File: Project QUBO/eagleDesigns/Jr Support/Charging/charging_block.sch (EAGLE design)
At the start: 123 parts

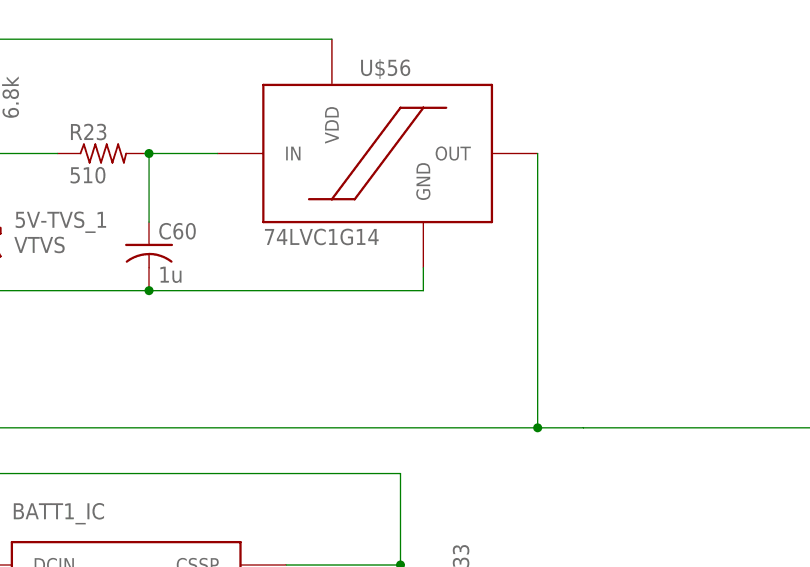
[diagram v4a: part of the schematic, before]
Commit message: 
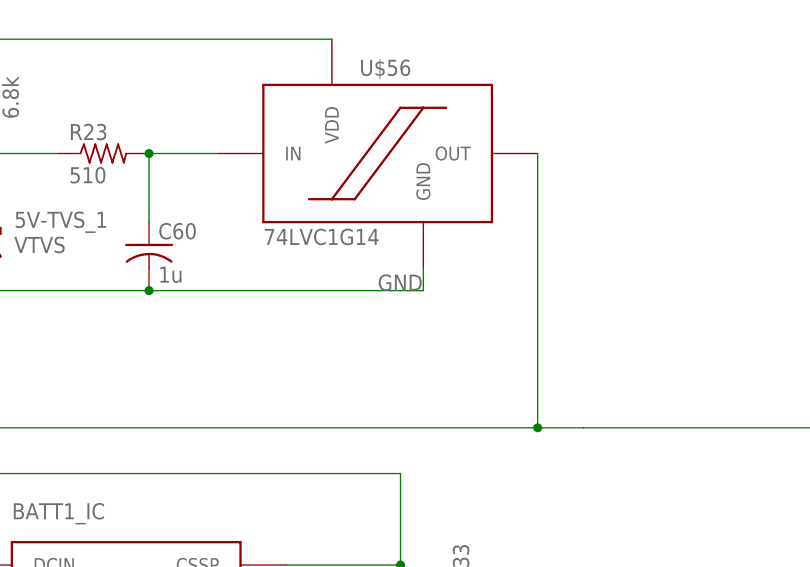
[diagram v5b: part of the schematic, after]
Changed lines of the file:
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@@
 <grid distance="0.1" unitdist="inch" unit="inch" style="lines" multiple="1" display="no" altdistance="0.01" altunitdist="inch" altunit="inch"/>
 <layers>
-<layer number="1" name="Top" color="4" fill="1" visible="yes" active="no"/>
-<layer number="2" name="Route2" color="1" fill="3" visible="yes" active="no"/>
-<layer number="3" name="Route3" color="4" fill="3" visible="yes" active="no"/>
-<layer number="4" name="Route4" color="1" fill="4" visible="yes" active="no"/>
-<layer number="5" name="Route5" color="4" fill="4" visible="yes" active="no"/>
-<layer number="6" name="Route6" color="1" fill="8" visible="yes" active="no"/>
-<layer number="7" name="Route7" color="4" fill="8" visible="yes" active="no"/>
-<layer number="8" name="Route8" color="1" fill="2" visible="yes" active="no"/>
-<layer number="9" name="Route9" color="4" fill="2" visible="yes" active="no"/>
-<layer number="10" name="Route10" color="1" fill="7" visible="yes" active="no"/>
-<layer number="11" name="Route11" color="4" fill="7" visible="yes" active="no"/>
-<layer number="12" name="Route12" color="1" fill="5" visible="yes" active="no"/>
-<layer number="13" name="Route13" color="4" fill="5" visible="yes" active="no"/>
-<layer number="14" name="Route14" color="1" fill="6" visible="yes" active="no"/>
-<layer number="15" name="Route15" color="4" fill="6" visible="yes" active="no"/>
-<layer number="16" name="Bottom" color="1" fill="12" visible="yes" active="no"/>
-<layer number="17" name="Pads" color="2" fill="1" visible="yes" active="no"/>
-<layer number="18" name="Vias" color="2" fill="1" visible="yes" active="no"/>
-<layer number="19" name="Unrouted" color="6" fill="1" visible="yes" active="no"/>
-<layer number="20" name="Dimension" color="15" fill="1" visible="yes" active="no"/>
-<layer number="21" name="tPlace" color="14" fill="1" visible="yes" active="no"/>
-<layer number="22" name="bPlace" color="7" fill="1" visible="yes" active="no"/>
-<layer number="23" name="tOrigins" color="15" fill="1" visible="yes" active="no"/>
-<layer number="24" name="bOrigins" color="15" fill="1" visible="yes" active="no"/>
-<layer number="25" name="tNames" color="7" fill="1" visible="yes" active="no"/>
-<layer number="26" name="bNames" color="7" fill="1" visible="yes" active="no"/>
-<layer number="27" name="tValues" color="7" fill="1" visible="yes" active="no"/>
-<layer number="28" name="bValues" color="7" fill="1" visible="yes" active="no"/>
+<layer number="1" name="Top" color="4" fill="1" visible="no" active="no"/>
+<layer number="2" name="Route2" color="1" fill="3" visible="no" active="no"/>
+<layer number="3" name="Route3" color="4" fill="3" visible="no" active="no"/>
+<layer number="4" name="Route4" color="1" fill="4" visible="no" active="no"/>
+<layer number="5" name="Route5" color="4" fill="4" visible="no" active="no"/>
+<layer number="6" name="Route6" color="1" fill="8" visible="no" active="no"/>
+<layer number="7" name="Route7" color="4" fill="8" visible="no" active="no"/>
+<layer number="8" name="Route8" color="1" fill="2" visible="no" active="no"/>
+<layer number="9" name="Route9" color="4" fill="2" visible="no" active="no"/>
+<layer number="10" name="Route10" color="1" fill="7" visible="no" active="no"/>
+<layer number="11" name="Route11" color="4" fill="7" visible="no" active="no"/>
+<layer number="12" name="Route12" color="1" fill="5" visible="no" active="no"/>
+<layer number="13" name="Route13" color="4" fill="5" visible="no" active="no"/>
+<layer number="14" name="Route14" color="1" fill="6" visible="no" active="no"/>
+<layer number="15" name="Route15" color="4" fill="6" visible="no" active="no"/>
+<layer number="16" name="Bottom" color="1" fill="12" visible="no" active="no"/>
+<layer number="17" name="Pads" color="2" fill="1" visible="no" active="no"/>
+<layer number="18" name="Vias" color="2" fill="1" visible="no" active="no"/>
+<layer number="19" name="Unrouted" color="6" fill="1" visible="no" active="no"/>
+<layer number="20" name="Dimension" color="15" fill="1" visible="no" active="no"/>
+<layer number="21" name="tPlace" color="14" fill="1" visible="no" active="no"/>
+<layer number="22" name="bPlace" color="7" fill="1" visible="no" active="no"/>
+<layer number="23" name="tOrigins" color="15" fill="1" visible="no" active="no"/>
+<layer number="24" name="bOrigins" color="15" fill="1" visible="no" active="no"/>
+<layer number="25" name="tNames" color="7" fill="1" visible="no" active="no"/>
+<layer number="26" name="bNames" color="7" fill="1" visible="no" active="no"/>
+<layer number="27" name="tValues" color="7" fill="1" visible="no" active="no"/>
+<layer number="28" name="bValues" color="7" fill="1" visible="no" active="no"/>
 <layer number="29" name="tStop" color="7" fill="3" visible="no" active="no"/>
 <layer number="30" name="bStop" color="7" fill="6" visible="no" active="no"/>
@@
 <layer number="35" name="tGlue" color="7" fill="4" visible="no" active="no"/>
 <layer number="36" name="bGlue" color="7" fill="5" visible="no" active="no"/>
-<layer number="37" name="tTest" color="7" fill="1" visible="yes" active="no"/>
-<layer number="38" name="bTest" color="7" fill="1" visible="yes" active="no"/>
+<layer number="37" name="tTest" color="7" fill="1" visible="no" active="no"/>
+<layer number="38" name="bTest" color="7" fill="1" visible="no" active="no"/>
 <layer number="39" name="tKeepout" color="4" fill="11" visible="no" active="no"/>
 <layer number="40" name="bKeepout" color="1" fill="11" visible="no" active="no"/>
@@
 <layer number="44" name="Drills" color="7" fill="1" visible="no" active="no"/>
 <layer number="45" name="Holes" color="7" fill="1" visible="no" active="no"/>
-<layer number="46" name="Milling" color="3" fill="1" visible="yes" active="no"/>
-<layer number="47" name="Measures" color="7" fill="1" visible="yes" active="no"/>
-<layer number="48" name="Document" color="7" fill="1" visible="yes" active="no"/>
-<layer number="49" name="Reference" color="7" fill="1" visible="yes" active="no"/>
-<layer number="50" name="dxf" color="7" fill="1" visible="yes" active="no"/>
-<layer number="51" name="tDocu" color="7" fill="1" visible="yes" active="no"/>
-<layer number="52" name="bDocu" color="7" fill="1" visible="yes" active="no"/>
-<layer number="53" name="tGND_GNDA" color="7" fill="9" visible="yes" active="no"/>
-<layer number="54" name="bGND_GNDA" color="1" fill="9" visible="yes" active="no"/>
-<layer number="56" name="wert" color="7" fill="1" visible="yes" active="no"/>
-<layer number="57" name="tCAD" color="7" fill="1" visible="yes" active="no"/>
-<layer number="59" name="tCarbon" color="7" fill="1" visible="yes" active="no"/>
-<layer number="60" name="bCarbon" color="7" fill="1" visible="yes" active="no"/>
+<layer number="46" name="Milling" color="3" fill="1" visible="no" active="no"/>
+<layer number="47" name="Measures" color="7" fill="1" visible="no" active="no"/>
+<layer number="48" name="Document" color="7" fill="1" visible="no" active="no"/>
+<layer number="49" name="Reference" color="7" fill="1" visible="no" active="no"/>
+<layer number="50" name="dxf" color="7" fill="1" visible="no" active="no"/>
+<layer number="51" name="tDocu" color="7" fill="1" visible="no" active="no"/>
+<layer number="52" name="bDocu" color="7" fill="1" visible="no" active="no"/>
+<layer number="53" name="tGND_GNDA" color="7" fill="9" visible="no" active="no"/>
+<layer number="54" name="bGND_GNDA" color="1" fill="9" visible="no" active="no"/>
+<layer number="56" name="wert" color="7" fill="1" visible="no" active="no"/>
+<layer number="57" name="tCAD" color="7" fill="1" visible="no" active="no"/>
+<layer number="59" name="tCarbon" color="7" fill="1" visible="no" active="no"/>
+<layer number="60" name="bCarbon" color="7" fill="1" visible="no" active="no"/>
 <layer number="90" name="Modules" color="5" fill="1" visible="yes" active="yes"/>
 <layer number="91" name="Nets" color="2" fill="1" visible="yes" active="yes"/>
@@
 <pinref part="5V-TVS_1" gate="G$1" pin="A"/>
 <junction x="76.2" y="114.3"/>
+<label x="119.38" y="111.76" size="1.778" layer="95"/>
 </segment>
 </net>

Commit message: 
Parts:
- R29, R34, R5, R7: device resistor:R-US_R0805 -> resistor:R-US_R2512
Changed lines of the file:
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@@
 <?xml version="1.0" encoding="utf-8"?>
 <!DOCTYPE eagle SYSTEM "eagle.dtd">
-<eagle version="8.1.0">
+<eagle version="8.2.0">
 <drawing>
 <settings>
@@
 <part name="C78" library="resistor" deviceset="C-US" device="C0805" value="0.1u"/>
 <part name="C79" library="resistor" deviceset="C-US" device="C0805" value="0.1u"/>
-<part name="R34" library="resistor" deviceset="R-US_" device="R0805" value="100m"/>
+<part name="R34" library="resistor" deviceset="R-US_" device="R2512" value="100m"/>
 <part name="C82" library="resistor" deviceset="C-US" device="C0805" value="0.1u"/>
 <part name="C83" library="resistor" deviceset="C-US" device="C0805" value="0.1u"/>
 <part name="C84" library="resistor" deviceset="CPOL-US" device="E3.5-8" value="120u"/>
-<part name="R29" library="resistor" deviceset="R-US_" device="R0805" value="100m"/>
+<part name="R29" library="resistor" deviceset="R-US_" device="R2512" value="100m"/>
 <part name="B1-ZENER" library="diode" deviceset="SCHOTTKY-DIODE" device="SOD-106"/>
 <part name="D1" library="diode" deviceset="DIODE-" device="SOD123"/>
@@
 <part name="C13" library="resistor" deviceset="C-US" device="C0805" value="0.1u"/>
 <part name="C14" library="resistor" deviceset="C-US" device="C0805" value="0.1u"/>
-<part name="R5" library="resistor" deviceset="R-US_" device="R0805" value="100m"/>
+<part name="R5" library="resistor" deviceset="R-US_" device="R2512" value="100m"/>
 <part name="C17" library="resistor" deviceset="C-US" device="C0805" value="0.1u"/>
 <part name="C18" library="resistor" deviceset="C-US" device="C0805" value="0.1u"/>
 <part name="C19" library="resistor" deviceset="CPOL-US" device="E3.5-8" value="120uF"/>
-<part name="R7" library="resistor" deviceset="R-US_" device="R0805" value="100m"/>
+<part name="R7" library="resistor" deviceset="R-US_" device="R2512" value="100m"/>
 <part name="U$5" library="diode" deviceset="SCHOTTKY-DIODE" device="SOD-106"/>
 <part name="D2" library="diode" deviceset="DIODE-" device="SOD123"/>
